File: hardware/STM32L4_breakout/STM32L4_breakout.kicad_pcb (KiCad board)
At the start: 2 copper layers, 84.8 x 91.2 mm, 66 parts, among them J1 12V IN, J10 GPIO, J12 USART1, J13 USART3, J15 3.3V, J16 5V, J17 12V, J2 SWD, J3 Conn_01x08, J4 Conn_01x06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

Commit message: breakout board power routing WIP
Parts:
- moved C15 2.49 mm to (137.9, 67.5)
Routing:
- net GND: track 18.5 -> 29.7 mm, vias 0 -> 8
- net SWDIO: track 18.1 -> 21.2 mm
- net STM_NRST: track 186.9 -> 189.9 mm
- net D7: track 55.9 -> 56.7 mm
- net TFT_DC: track 81.5 -> 82.1 mm

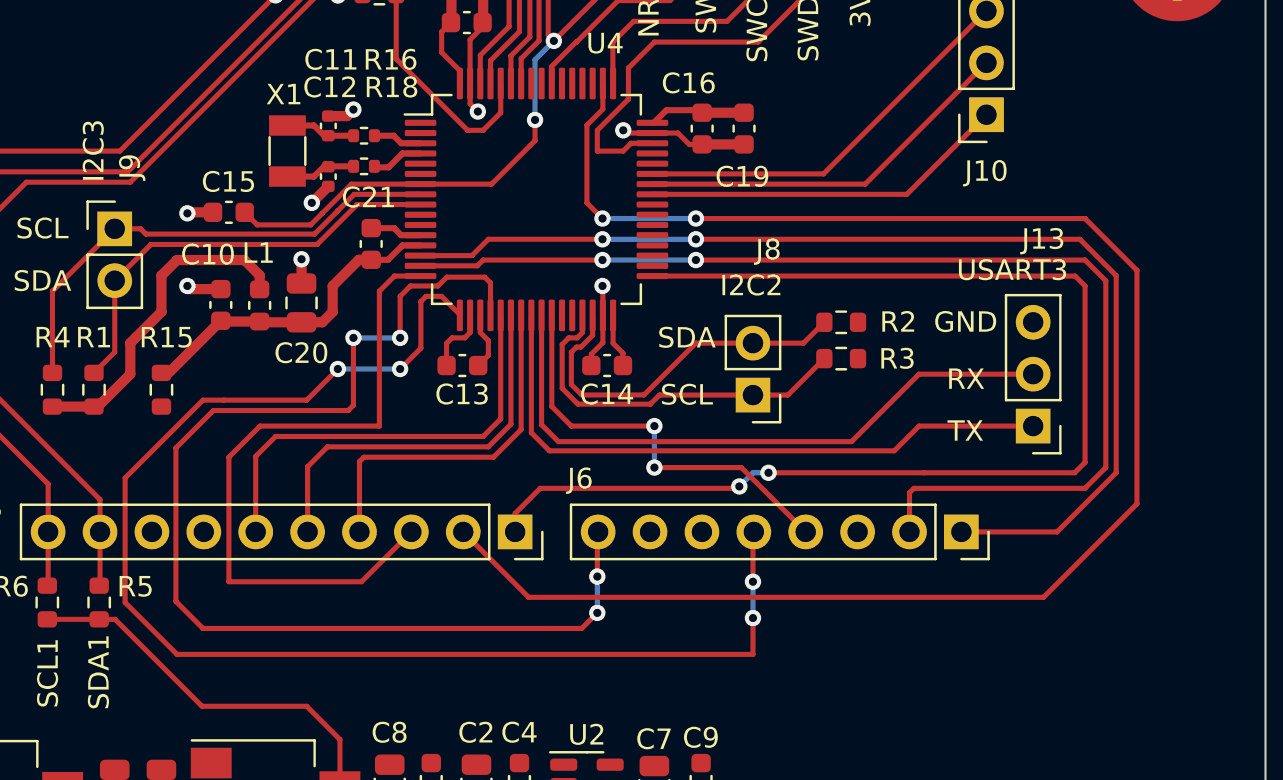
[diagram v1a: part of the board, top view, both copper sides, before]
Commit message: breakout board re-routed D7
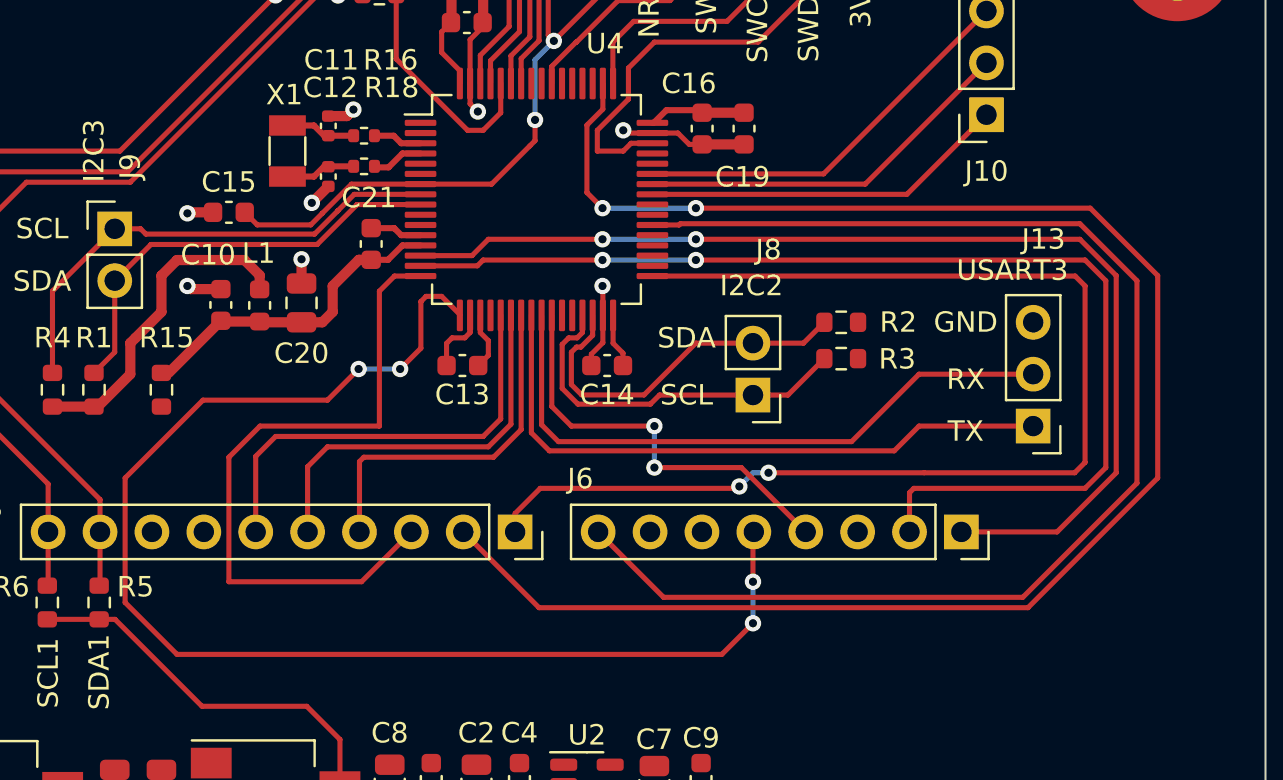
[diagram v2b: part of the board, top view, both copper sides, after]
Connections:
- U4 pad 20: D7 -> unconnected-(U4-Pad20)
- U4 pad 38: unconnected-(U4-Pad38) -> D7
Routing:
- net D7: track 56.7 -> 64.9 mm, vias 4 -> 0
- net TFT_DC: track 82.1 -> 83.4 mm
- net CARDCS_5V: track 65.7 -> 64.8 mm

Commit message: breakout board power routing WIP
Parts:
- moved C7 4.06 mm to (162.8, 95.6)
- moved C9 4.06 mm to (165.1, 95.2)
- moved U2 3.56 mm to (159.0, 95.5)
- moved C6 3.50 mm to (161.0, 98.6)
- moved C2 3.05 mm to (153.1, 95.5)
- moved C4 3.05 mm to (155.2, 95.2)
- moved C22 2.03 mm to (149.9, 95.2)
- moved C8 2.03 mm to (147.8, 95.5)
- moved U3 1.27 mm to (141.5, 96.8)
- moved C3 0.61 mm to (132.9, 95.8)
- moved C5 0.61 mm to (135.2, 95.8)
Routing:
- net +3.3V: track 52.1 -> 34.4 mm
- net GND: track 29.7 -> 31.3 mm, vias 8 -> 30
- added copper zone on F.Cu, net +12V
- added copper zone on F.Cu, net GND

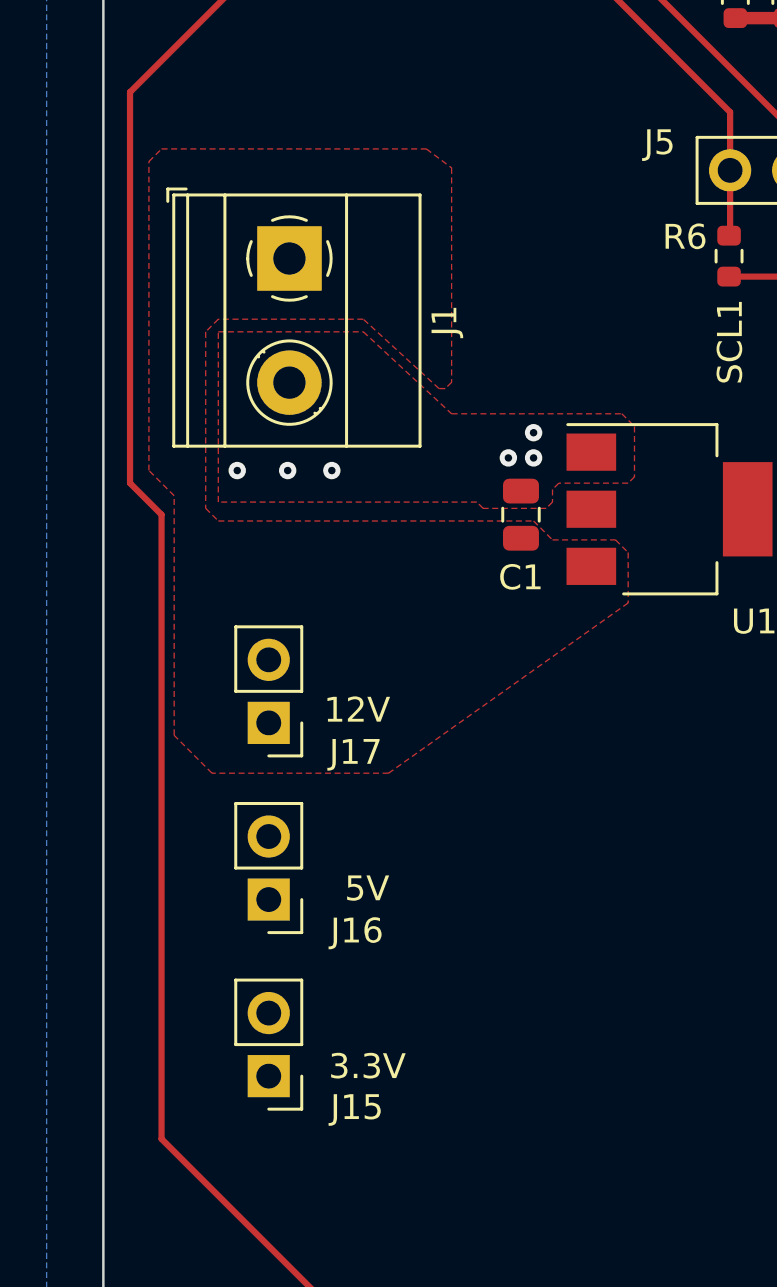
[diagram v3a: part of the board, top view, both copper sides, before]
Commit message: added pwr indicator LEDs
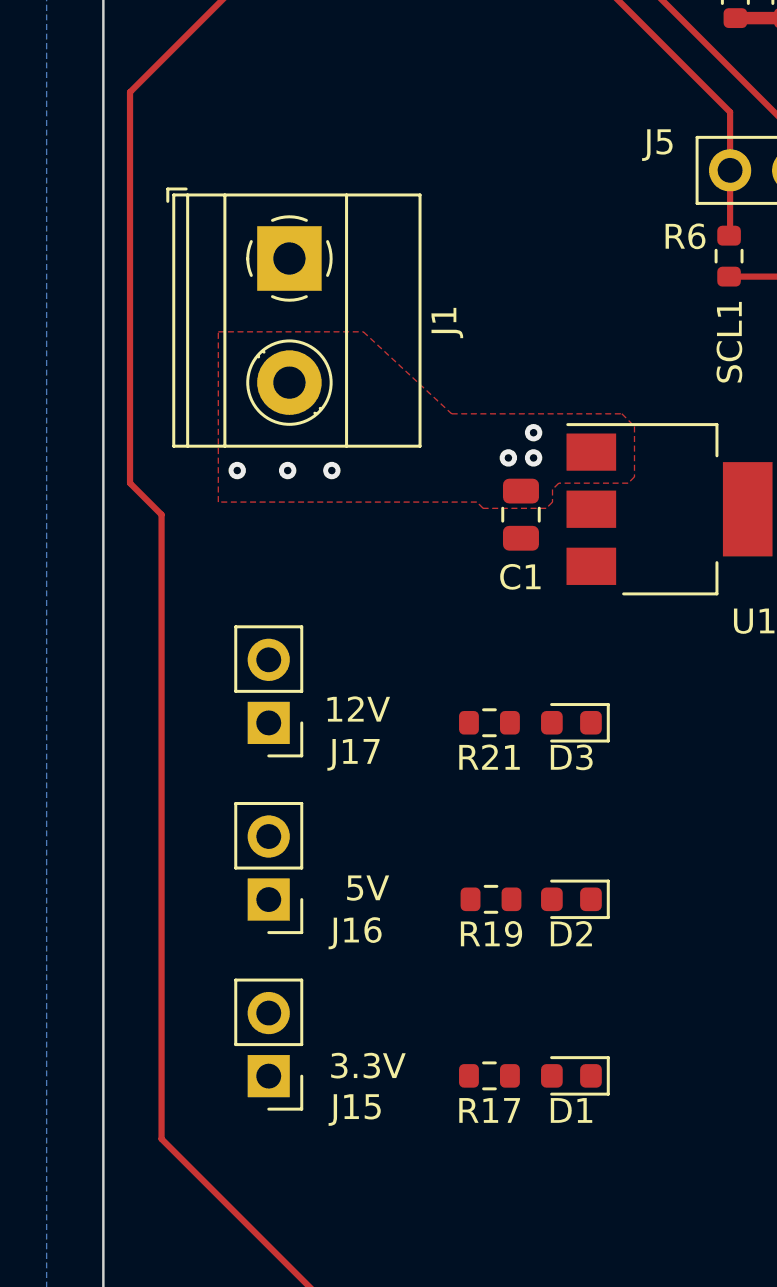
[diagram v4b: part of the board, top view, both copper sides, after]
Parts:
- added D1: LED_Green, LED_SMD:LED_0603_1608Metric, F.Cu at (122.7, 119.6)
- added D2: LED_Green, LED_SMD:LED_0603_1608Metric, F.Cu at (122.7, 112.5)
- added D3: LED_Green, LED_SMD:LED_0603_1608Metric, F.Cu at (122.7, 105.4)
- added R17: 330R, Resistor_SMD:R_0603_1608Metric, F.Cu at (119.4, 119.6)
- added R19: 330R, Resistor_SMD:R_0603_1608Metric, F.Cu at (119.4, 112.5)
- added R21: 330R, Resistor_SMD:R_0603_1608Metric, F.Cu at (119.4, 105.4)
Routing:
- removed copper zone on F.Cu, net +12V

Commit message: breakout board power routing WIP
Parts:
- moved J15 72.6 mm to (180.1, 98.8)
- moved R17 62.1 mm to (179.1, 102.6), turned to 90 degrees
- moved D1 60.8 mm to (181.1, 102.6), turned to -90 degrees
- moved C6 22.4 mm to (141.6, 109.7)
- moved C7 22.4 mm to (143.3, 106.7)
- moved C2 22.4 mm to (133.6, 106.6)
- moved C4 22.4 mm to (135.7, 106.4)
- moved C9 22.4 mm to (145.6, 106.4)
- moved U2 22.4 mm to (139.5, 106.6)
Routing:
- net +3.3V: track 34.4 -> 53.1 mm
- net GND: track 31.3 -> 35.8 mm, vias 30 -> 33
- net /3V3_LED: track 0.00 -> 2.05 mm
- net /12V_LED: track 0.00 -> 1.69 mm
- net /5V_LED: track 0.00 -> 1.63 mm
- added copper zone on F.Cu, net +12V
- added copper zone on F.Cu, net +3.3V
- added copper zone on F.Cu, net +5V
- added copper zone on F.Cu, net VMEM

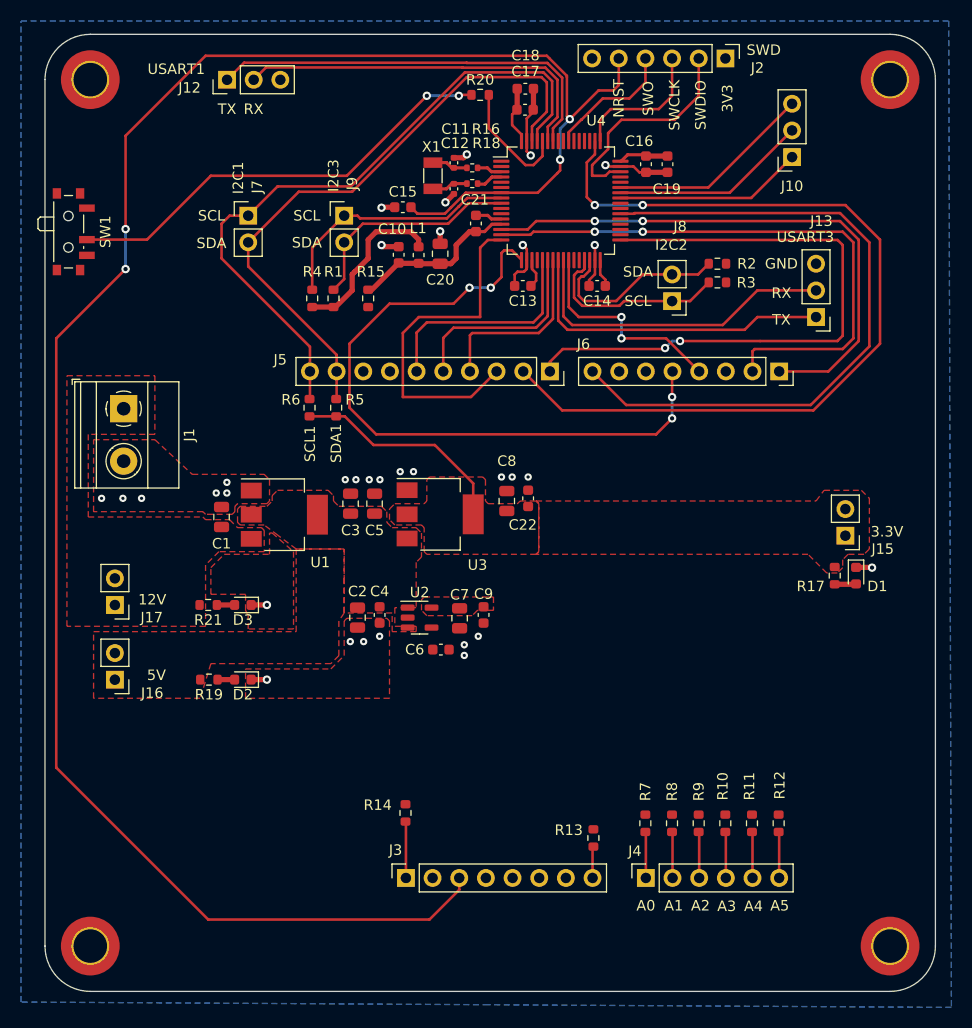
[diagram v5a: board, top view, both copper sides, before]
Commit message: Breakout Board PCB power routing WIP
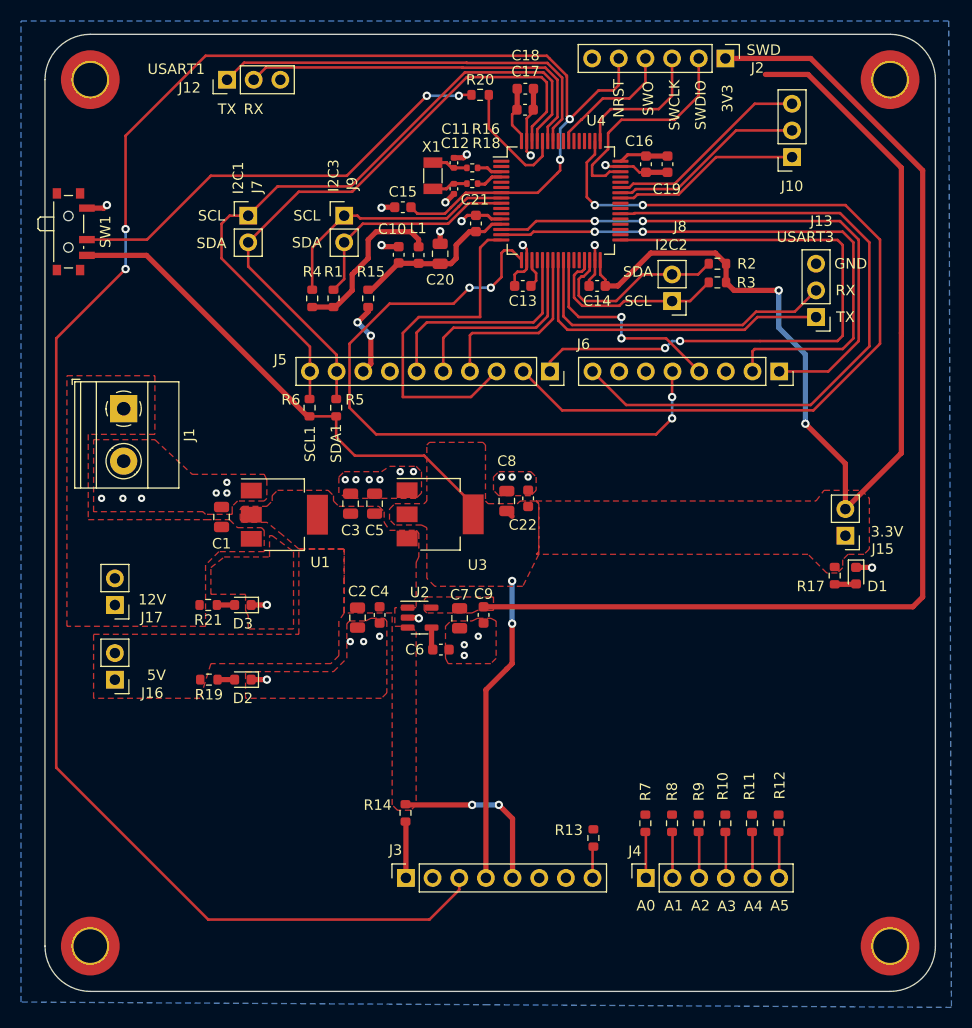
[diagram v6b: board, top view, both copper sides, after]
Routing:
- net +3.3V: track 53.1 -> 205.8 mm, vias 0 -> 4
- net VMEM: track 0.00 -> 106.1 mm
- net +5V: track 0.00 -> 16.4 mm, vias 0 -> 2
- net /ARD_3V3A: track 0.00 -> 7.38 mm, vias 0 -> 2
- net GND: track 35.8 -> 40.5 mm, vias 33 -> 36
- net Net-(C6-Pad1): track 0.00 -> 2.15 mm
